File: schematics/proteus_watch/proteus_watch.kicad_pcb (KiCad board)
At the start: 4 copper layers, 47.6 x 23.7 mm, 96 parts, among them J1 2167010509_MOLEX, J2 SOLDER PAD, J3 SOLDER PAD, J4 UJ20-C-H-G-SMT-2A-P16-TR, J5 2167010509_MOLEX, Q2 RE1C002UN, Q3 RE1C002UN, Q4 S8050, Q5 S8050, SW1 R-667995, SW2 R-667995, SW3 EVQ-P7A01P, SW4 EVQ-P7A01P, SW5 EVQ-P7A01P, U1 MAX17048G+T10, U10 LSM6DSO, U11 BQ25185, U12 NCP186AMX330TAG, U13 CP2102N-Axx-xQFN28, U3 MIC2876-5.0YMT-TR, U4 MIC5365-1.8YMT-TZ, U5 NCP186AMX330TAG, U6 ESP32-S3-MINI-1, U7 MAX30101EFD_T, U8 PCF85063ATL, Y1 32.768kHZ, 7pF, 60kOhms

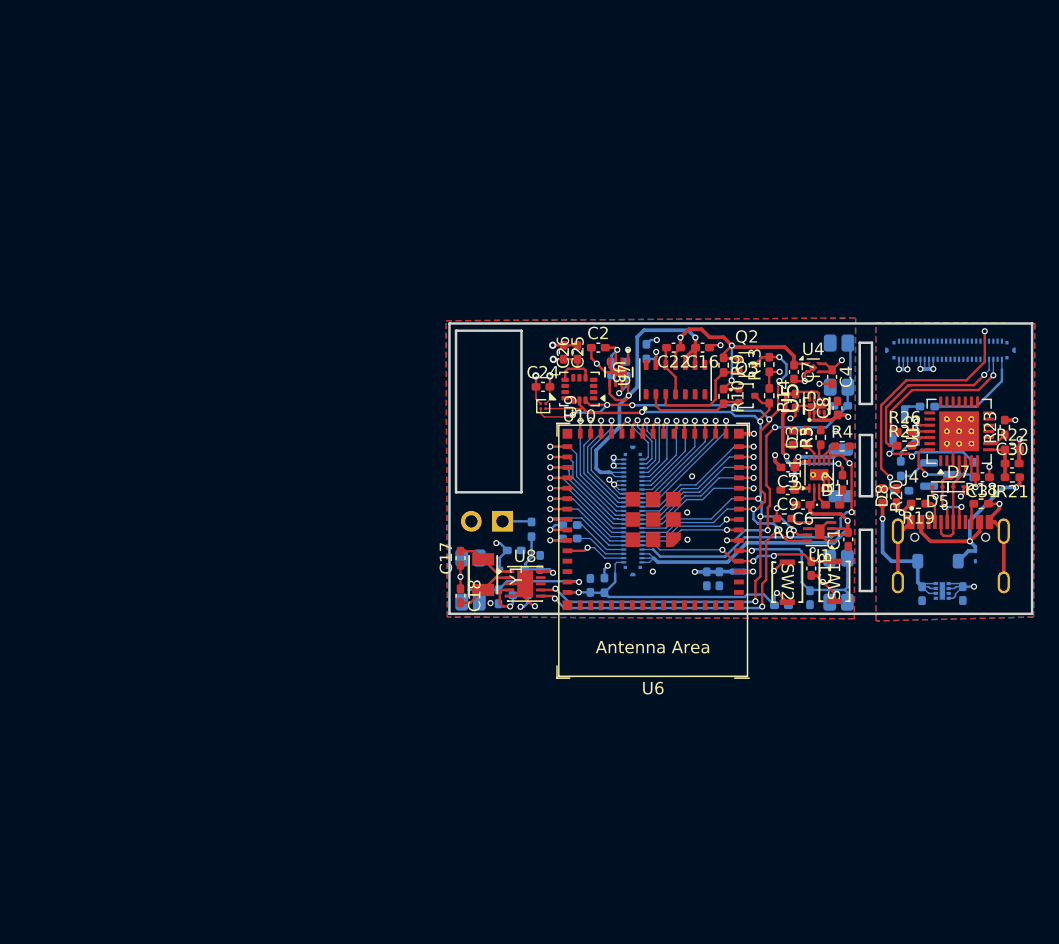
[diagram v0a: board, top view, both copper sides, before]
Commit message: v1.3
progress update with PCB layout. Repurposing old board design.
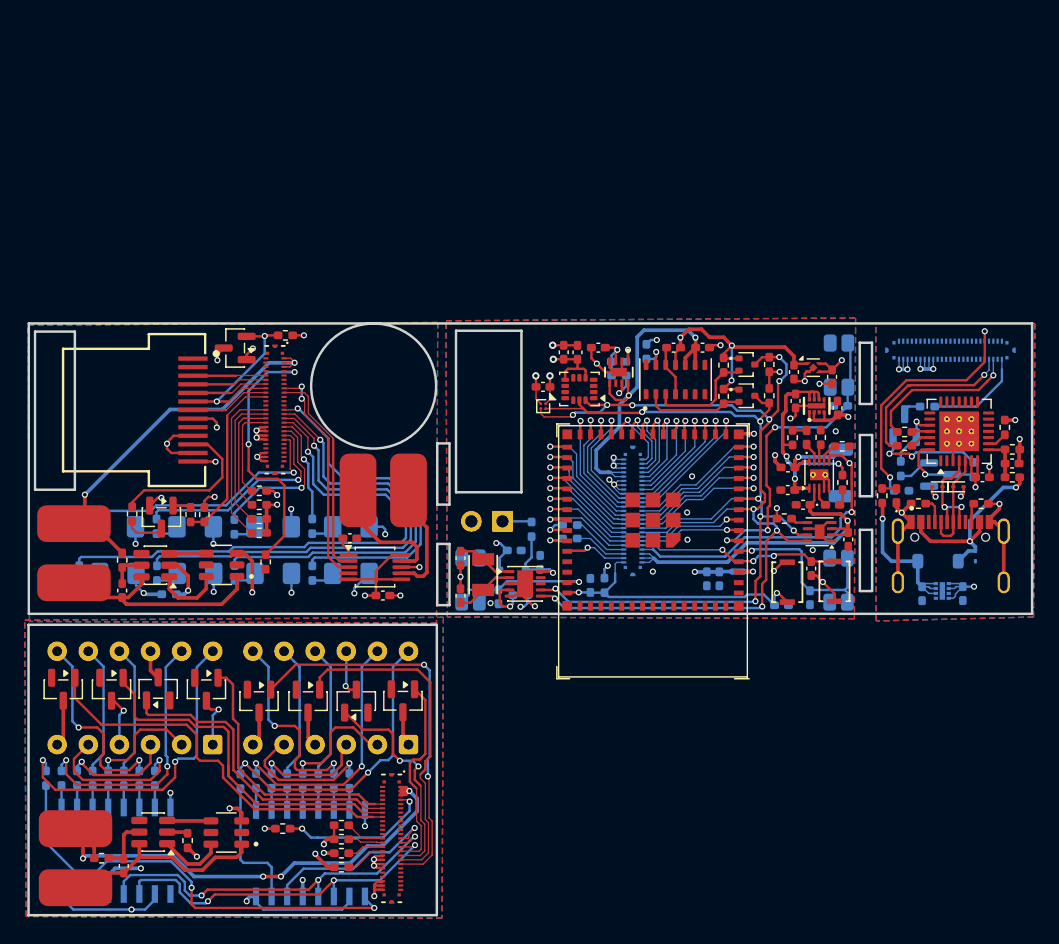
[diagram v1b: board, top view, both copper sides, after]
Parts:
- added C33: 1uF, Capacitor_SMD:C_0402_1005Metric_Pad0.74x0.62mm_HandSolder, F.Cu at (114.2, 119.4)
- added C34: 0.1uF, Capacitor_SMD:C_0402_1005Metric_Pad0.74x0.62mm_HandSolder, F.Cu at (93.0, 119.0)
- added C35: 1uF, Capacitor_SMD:C_0402_1005Metric_Pad0.74x0.62mm_HandSolder, F.Cu at (111.5, 114.7)
- added C36: 0.1uF, Capacitor_SMD:C_0402_1005Metric_Pad0.74x0.62mm_HandSolder, F.Cu at (93.1, 141.5)
- added D11: LED, LED_SMD:LED_1206_3216Metric_Pad1.42x1.75mm_HandSolder, B.Cu at (92.6, 113.8)
- added D12: LED, LED_SMD:LED_1206_3216Metric_Pad1.42x1.75mm_HandSolder, B.Cu at (98.9, 113.8)
- added D13: LED, LED_SMD:LED_1206_3216Metric_Pad1.42x1.75mm_HandSolder, B.Cu at (105.3, 113.8)
- added D14: LED, LED_SMD:LED_1206_3216Metric_Pad1.42x1.75mm_HandSolder, B.Cu at (111.6, 113.8)
- added D15: LED, LED_SMD:LED_1206_3216Metric_Pad1.42x1.75mm_HandSolder, B.Cu at (92.6, 117.6)
- added D16: LED, LED_SMD:LED_1206_3216Metric_Pad1.42x1.75mm_HandSolder, B.Cu at (98.9, 117.6)
- added D17: LED, LED_SMD:LED_1206_3216Metric_Pad1.42x1.75mm_HandSolder, B.Cu at (105.3, 117.6)
- added D18: LED, LED_SMD:LED_1206_3216Metric_Pad1.42x1.75mm_HandSolder, B.Cu at (111.6, 117.6)
- added J10: BAT+, Connector_Wire:SolderWirePad_1x01_SMD_3x6mm, F.Cu at (89.0, 113.5)
- added J11: BAT-, Connector_Wire:SolderWirePad_1x01_SMD_3x6mm, F.Cu at (89.0, 118.4)
- added J12: BAT+, Connector_Wire:SolderWirePad_1x01_SMD_3x6mm, F.Cu at (89.2, 138.4)
- added J13: BAT-, Connector_Wire:SolderWirePad_1x01_SMD_3x6mm, F.Cu at (89.2, 143.3)
- added J14: 2167010509_MOLEX, footprint:CON_2167010509_MOL, F.Cu at (115.0, 139.2)
- added J7: 2167010509_MOLEX, footprint:CON_2167010509_MOL, F.Cu at (105.4, 104.2)
- added J8: MOTOR+, Connector_Wire:SolderWirePad_1x01_SMD_3x6mm, F.Cu at (116.3, 110.8)
- added J9: MOTOR-, Connector_Wire:SolderWirePad_1x01_SMD_3x6mm, F.Cu at (112.2, 110.8)
- added Q10: MMBT2222ALT3G, Package_TO_SOT_SMD:SOT-23, F.Cu at (112.1, 128.0)
- added Q11: MMBT2222ALT3G, Package_TO_SOT_SMD:SOT-23, F.Cu at (108.1, 128.0)
- added Q12: MMBT2222ALT3G, Package_TO_SOT_SMD:SOT-23, F.Cu at (104.1, 128.0)
- added Q13: MMBT2222ALT3G, Package_TO_SOT_SMD:SOT-23, F.Cu at (99.8, 127.1)
- added Q14: MMBT2222ALT3G, Package_TO_SOT_SMD:SOT-23, F.Cu at (95.9, 127.0)
- added Q15: MMBT2222ALT3G, Package_TO_SOT_SMD:SOT-23, F.Cu at (92.1, 127.1)
- added Q16: MMBT2222ALT3G, Package_TO_SOT_SMD:SOT-23, F.Cu at (88.2, 127.1)
- added Q6: MMBT2222ALT3G, Package_TO_SOT_SMD:SOT-23, F.Cu at (96.2, 113.0)
- added Q7: FS8205, footprint:SOT95P280X145-6N, F.Cu at (101.1, 116.9)
- added Q8: FS8205, footprint:SOT95P280X145-6N, F.Cu at (101.5, 138.8)
- added Q9: MMBT2222ALT3G, Package_TO_SOT_SMD:SOT-23, F.Cu at (115.9, 128.0)
- added R33: 1K, Resistor_SMD:R_0402_1005Metric_Pad0.72x0.64mm_HandSolder, F.Cu at (98.6, 112.8)
- added R34: 22, Resistor_SMD:R_0402_1005Metric_Pad0.72x0.64mm_HandSolder, F.Cu at (93.8, 112.8)
- added R35: 10K, Resistor_SMD:R_0402_1005Metric_Pad0.72x0.64mm_HandSolder, F.Cu at (99.7, 112.8)
- added R36: 10K, Resistor_SMD:R_0402_1005Metric_Pad0.72x0.64mm_HandSolder, F.Cu at (106.3, 98.2)
- added R37: 180, Resistor_SMD:R_0402_1005Metric_Pad0.72x0.64mm_HandSolder, B.Cu at (89.4, 113.8)
- added R38: 180, Resistor_SMD:R_0402_1005Metric_Pad0.72x0.64mm_HandSolder, B.Cu at (95.8, 113.8)
- added R39: 180, Resistor_SMD:R_0402_1005Metric_Pad0.72x0.64mm_HandSolder, B.Cu at (102.1, 113.8)
- added R40: 180, Resistor_SMD:R_0402_1005Metric_Pad0.72x0.64mm_HandSolder, B.Cu at (108.5, 113.8)
- added R41: 180, Resistor_SMD:R_0402_1005Metric_Pad0.72x0.64mm_HandSolder, B.Cu at (89.5, 117.6)
- added R42: 180, Resistor_SMD:R_0402_1005Metric_Pad0.72x0.64mm_HandSolder, B.Cu at (95.8, 117.6)
- added R43: 180, Resistor_SMD:R_0402_1005Metric_Pad0.72x0.64mm_HandSolder, B.Cu at (102.1, 117.6)
- added R44: 180, Resistor_SMD:R_0402_1005Metric_Pad0.72x0.64mm_HandSolder, B.Cu at (108.5, 117.6)
- added R45: 100, Resistor_SMD:R_0402_1005Metric_Pad0.72x0.64mm_HandSolder, F.Cu at (93.0, 116.5)
- added R46: 1K, Resistor_SMD:R_0402_1005Metric_Pad0.72x0.64mm_HandSolder, B.Cu at (96.8, 119.3)
- added R47: 10K, Resistor_SMD:R_0402_1005Metric_Pad0.72x0.64mm_HandSolder, F.Cu at (104.2, 110.9)
- added R48: 10K, Resistor_SMD:R_0402_1005Metric_Pad0.72x0.64mm_HandSolder, F.Cu at (104.2, 112.0)
- added R49: 10K, Resistor_SMD:R_0402_1005Metric_Pad0.72x0.64mm_HandSolder, F.Cu at (104.2, 113.1)
- added R50: 10K, Resistor_SMD:R_0402_1005Metric_Pad0.72x0.64mm_HandSolder, F.Cu at (104.2, 114.3)
- added R51: 100, Resistor_SMD:R_0402_1005Metric_Pad0.72x0.64mm_HandSolder, F.Cu at (91.3, 140.8)
- added R52: 1K, Resistor_SMD:R_0402_1005Metric_Pad0.72x0.64mm_HandSolder, F.Cu at (98.3, 139.4)
- added R53: 10K, Resistor_SMD:R_0402_1005Metric_Pad0.72x0.64mm_HandSolder, F.Cu at (110.9, 138.2)
- added R54: 10K, Resistor_SMD:R_0402_1005Metric_Pad0.72x0.64mm_HandSolder, F.Cu at (110.9, 139.3)
- added R55: 10K, Resistor_SMD:R_0402_1005Metric_Pad0.72x0.64mm_HandSolder, F.Cu at (110.9, 140.4)
- added R56: 10K, Resistor_SMD:R_0402_1005Metric_Pad0.72x0.64mm_HandSolder, F.Cu at (110.9, 141.6)
- added R57: 360, Resistor_SMD:R_0402_1005Metric_Pad0.72x0.64mm_HandSolder, B.Cu at (102.6, 134.6)
- added R58: 360, Resistor_SMD:R_0402_1005Metric_Pad0.72x0.64mm_HandSolder, B.Cu at (103.9, 134.5)
- added R59: 360, Resistor_SMD:R_0402_1005Metric_Pad0.72x0.64mm_HandSolder, B.Cu at (105.2, 134.5)
- added R60: 360, Resistor_SMD:R_0402_1005Metric_Pad0.72x0.64mm_HandSolder, B.Cu at (106.4, 134.5)
- added R61: 360, Resistor_SMD:R_0402_1005Metric_Pad0.72x0.64mm_HandSolder, B.Cu at (107.7, 134.5)
- added R62: 360, Resistor_SMD:R_0402_1005Metric_Pad0.72x0.64mm_HandSolder, B.Cu at (109.0, 134.5)
- added R63: 360, Resistor_SMD:R_0402_1005Metric_Pad0.72x0.64mm_HandSolder, B.Cu at (110.2, 134.5)
- added R64: 360, Resistor_SMD:R_0402_1005Metric_Pad0.72x0.64mm_HandSolder, B.Cu at (111.5, 134.5)
- added R65: 360, Resistor_SMD:R_0402_1005Metric_Pad0.72x0.64mm_HandSolder, B.Cu at (86.7, 134.3)
- added R66: 360, Resistor_SMD:R_0402_1005Metric_Pad0.72x0.64mm_HandSolder, B.Cu at (88.0, 134.3)
- added R67: 360, Resistor_SMD:R_0402_1005Metric_Pad0.72x0.64mm_HandSolder, B.Cu at (89.3, 134.3)
- added R68: 360, Resistor_SMD:R_0402_1005Metric_Pad0.72x0.64mm_HandSolder, B.Cu at (90.6, 134.3)
- added R69: 360, Resistor_SMD:R_0402_1005Metric_Pad0.72x0.64mm_HandSolder, B.Cu at (91.8, 134.3)
- added R70: 360, Resistor_SMD:R_0402_1005Metric_Pad0.72x0.64mm_HandSolder, B.Cu at (93.1, 134.3)
- added R71: 360, Resistor_SMD:R_0402_1005Metric_Pad0.72x0.64mm_HandSolder, B.Cu at (94.4, 134.3)
- added R72: 360, Resistor_SMD:R_0402_1005Metric_Pad0.72x0.64mm_HandSolder, B.Cu at (95.6, 134.3)
- added TH1: 10K, Resistor_SMD:R_0402_1005Metric_Pad0.72x0.64mm_HandSolder, F.Cu at (104.7, 116.7)
- added TH2: 10K, Resistor_SMD:R_0402_1005Metric_Pad0.72x0.64mm_HandSolder, F.Cu at (106.1, 138.4)
- added U14: DRV2605LDGS, Package_SO:TSSOP-10_3x3mm_P0.5mm, F.Cu at (113.6, 117.1)
- added U15: DW01A, Package_TO_SOT_SMD:SOT-23-6, F.Cu at (95.7, 116.9)
- added U16: ~, Package_TO_SOT_SMD:SOT-23, F.Cu at (102.2, 99.2)
- added U17: ~, footprint:Wisevision N096-1608TBBIG11-H13, F.Cu at (98.7, 104.3)
- added U18: DW01A, Package_TO_SOT_SMD:SOT-23-6, F.Cu at (95.5, 138.7)
- added U19: ~, Package_DIP:DIP-12_W7.62mm, B.Cu at (100.4, 131.6)
- added U20: ~, Package_DIP:DIP-12_W7.62mm, B.Cu at (116.3, 131.6)
- added U21: SN74HC595NSR, footprint:NS16-L, B.Cu at (108.3, 140.4)
- added U22: SN74HC595NSR, footprint:NS16-L, B.Cu at (92.5, 140.2)
- moved U6 0.05 mm to (136.3, 113.2)
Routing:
- net /face1/GPIO13: track 0.00 -> 44.8 mm, vias 0 -> 1
- net /face2/BAT+: track 0.00 -> 40.3 mm, vias 0 -> 4
- net /face1/GPIO12: track 0.00 -> 39.5 mm, vias 0 -> 1
- net FRONT_GND: track 0.00 -> 35.7 mm, vias 0 -> 17
- net /face1/GPIO11: track 0.00 -> 34.0 mm, vias 0 -> 1
- net /face2/CAT2_4: track 0.00 -> 32.4 mm
- net /face2/CAT1_4: track 0.00 -> 32.2 mm, vias 0 -> 2
- net /face1/BAT+: track 0.00 -> 32.2 mm, vias 0 -> 2
- net /face2/GPIO11: track 0.00 -> 30.8 mm, vias 0 -> 3
- net /face2/CAT2_3: track 0.00 -> 30.3 mm
- net /face2/GPIO12: track 0.00 -> 29.3 mm, vias 0 -> 3
- net Net-(U21-QH'): track 0.00 -> 28.9 mm, vias 0 -> 2
- net /face1/GPIO10: track 0.00 -> 28.5 mm, vias 0 -> 1
- net /face2/CAT1_3: track 0.00 -> 27.7 mm
- net Net-(U19-ANODE_a): track 0.00 -> 26.3 mm, vias 0 -> 2
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- added copper zone on In2.Cu, net F2_3V3
- added copper zone on B.Cu, net F2_GND
- added copper zone on F.Cu, net F2_GND
- added copper zone on In1.Cu, net F2_GND
- added copper zone on In2.Cu, net FRONT_3V3
- added copper zone on B.Cu, net FRONT_GND
- added copper zone on F.Cu, net FRONT_GND
- added copper zone on In1.Cu, net FRONT_GND
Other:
- board size 47.6 x 23.7 mm -> 81.9 x 48.3 mm

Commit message: v1.31
wip integrating face3
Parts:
- added C37: 0.1uF, Capacitor_SMD:C_0402_1005Metric_Pad0.74x0.62mm_HandSolder, F.Cu at (145.2, 140.2)
- added DS1: HCMS-2901, Package_DIP:DIP-12_W7.62mm, B.Cu at (122.5, 135.1)
- added DS2: HCMS-2901, Package_DIP:DIP-12_W7.62mm, B.Cu at (122.5, 125.2)
- added J15: BAT+, Connector_Wire:SolderWirePad_1x01_SMD_3x6mm, F.Cu at (149.1, 143.3)
- added J16: BAT-, Connector_Wire:SolderWirePad_1x01_SMD_3x6mm, F.Cu at (149.1, 138.3)
- added J17: 2167010509_MOLEX, footprint:CON_2167010509_MOL, F.Cu at (145.0, 130.0)
- added Q17: FS8205, footprint:SOT95P280X145-6N, F.Cu at (139.0, 140.8)
- added R73: 100, Resistor_SMD:R_0402_1005Metric_Pad0.72x0.64mm_HandSolder, F.Cu at (147.0, 140.8)
- added R74: 10K, Resistor_SMD:R_0402_1005Metric_Pad0.72x0.64mm_HandSolder, F.Cu at (141.7, 127.1)
- added R75: 10K, Resistor_SMD:R_0402_1005Metric_Pad0.72x0.64mm_HandSolder, F.Cu at (141.7, 128.2)
- added R76: 10K, Resistor_SMD:R_0402_1005Metric_Pad0.72x0.64mm_HandSolder, F.Cu at (141.7, 129.4)
- added R77: 10K, Resistor_SMD:R_0402_1005Metric_Pad0.72x0.64mm_HandSolder, F.Cu at (141.7, 130.5)
- added R78: 1K, Resistor_SMD:R_0402_1005Metric_Pad0.72x0.64mm_HandSolder, F.Cu at (139.6, 143.5)
- added TH3: 10K, Resistor_SMD:R_0402_1005Metric_Pad0.72x0.64mm_HandSolder, F.Cu at (139.9, 133.8)
- added U23: DW01A, Package_TO_SOT_SMD:SOT-23-6, F.Cu at (143.0, 143.2)
- moved Q10 0.11 mm to (112.1, 128.1)
- moved Q11 0.11 mm to (108.1, 128.1)
- moved Q12 0.11 mm to (104.1, 128.1)
- moved Q14 0.11 mm to (95.9, 127.1)
- moved Q16 0.11 mm to (88.1, 127.2)
- moved Q8 0.11 mm to (101.4, 138.9)
- moved R52 0.11 mm to (98.3, 139.5)
- moved R57 0.11 mm to (102.6, 134.7)
- moved R59 0.11 mm to (105.1, 134.6)
- moved R60 0.11 mm to (106.4, 134.6)
- moved R61 0.11 mm to (107.7, 134.6)
- moved R63 0.11 mm to (110.2, 134.6)
- moved R64 0.11 mm to (111.5, 134.6)
- moved R65 0.11 mm to (86.7, 134.4)
- moved R67 0.11 mm to (89.3, 134.4)
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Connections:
- net Net-(J7-Pin_38) renamed /face1/GPIO48
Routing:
- net /face3/BAT+: track 0.00 -> 28.7 mm, vias 0 -> 4
- net Net-(J16-Pin_1): track 0.00 -> 17.4 mm
- net Net-(U23-OC): track 0.00 -> 6.67 mm
- net Net-(U23-VCC): track 0.00 -> 4.89 mm
- net /face3/GPIO48: track 0.00 -> 4.54 mm
- net /face3/GPIO34: track 0.00 -> 3.64 mm
- net /face3/GPIO33: track 0.00 -> 2.80 mm
- net /face3/GPIO47: track 0.00 -> 2.15 mm
- net F3_GND: track 0.00 -> 2.09 mm, vias 0 -> 2
- net Net-(U23-OD): track 0.00 -> 1.99 mm
- net Net-(U23-CS): track 0.00 -> 1.81 mm
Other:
- board size 81.9 x 48.3 mm -> 81.9 x 48.4 mm

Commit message: v1.4
completed board layout for production
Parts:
- moved C37 49.0 mm to (145.0, 91.2)
- moved DS1 49.0 mm to (122.4, 86.1)
- moved DS2 49.0 mm to (122.4, 76.1)
- moved R75 49.0 mm to (141.6, 79.2)
- moved TH3 49.0 mm to (139.7, 84.7), turned to 180 degrees
- moved J15 49.0 mm to (148.9, 94.2)
- moved J16 49.0 mm to (148.9, 89.3)
- moved J17 49.0 mm to (144.8, 80.9)
- moved Q17 49.0 mm to (138.9, 91.8)
- moved R73 49.0 mm to (146.8, 91.8)
- moved R74 49.0 mm to (141.6, 78.0)
- moved R76 49.0 mm to (141.6, 80.3)
- moved R77 49.0 mm to (141.6, 81.5)
- moved R78 49.0 mm to (139.4, 94.5)
- moved U23 49.0 mm to (142.8, 94.2)
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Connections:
- TH3 pad 2: F2_GND -> F3_GND
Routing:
- net /face3/GPIO10: track 0.00 -> 38.4 mm, vias 0 -> 1
- net /face3/GPIO11: track 0.00 -> 37.8 mm, vias 0 -> 1
- net /face3/GPIO12: track 0.00 -> 35.7 mm, vias 0 -> 1
- net /face3/CLK: track 0.00 -> 35.6 mm, vias 0 -> 2
- net /face3/GPIO14: track 0.00 -> 34.7 mm, vias 0 -> 1
- net GND: track 47.6 -> 80.4 mm, vias 22 -> 49
- net /face3/BLANK: track 0.00 -> 30.9 mm, vias 0 -> 1
- net /face3/DOUT: track 0.00 -> 27.5 mm, vias 0 -> 1
- net /face3/CE: track 0.00 -> 27.4 mm, vias 0 -> 1
- net /face3/DIN: track 0.00 -> 24.8 mm, vias 0 -> 1
- net Net-(DS1-DATA_IN): track 0.00 -> 17.1 mm
- net Net-(J17-Pin_4): track 0.00 -> 15.4 mm, vias 0 -> 2
- net F2_GND: track 20.8 -> 30.5 mm, vias 10 -> 49
- net F3_3V3: track 0.00 -> 8.01 mm
- net F3_GND: track 2.09 -> 9.56 mm, vias 2 -> 36
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- added copper zone on In2.Cu, net F3_5V
- added copper zone on B.Cu, net F3_GND
- added copper zone on F.Cu, net F3_GND
- added copper zone on In1.Cu, net F3_GND
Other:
- board size 81.9 x 48.4 mm -> 81.5 x 48.2 mm
